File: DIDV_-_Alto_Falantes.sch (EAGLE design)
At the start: 32 parts, among them J101 JACKP2, J102 JACKP2, U101 LM386M, U102 LM386M

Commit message: Revisão 7:
-  Alterações necessárias para adequação às necessidades dos exemplos de controle que temos.
-  Revisão da forma de filtragem de sinais digitais
-  Algumas nomenclaturas ainda estão erradas, deverão ser corrigidas com o andamento da implementação.
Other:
- note added: "07"
- note removed: "01"
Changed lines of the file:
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@@
 <text x="203.2" y="29.464" size="1.778" layer="150" font="vector">Dispositivo de Interface para</text>
 <text x="210.82" y="26.162" size="1.778" layer="150" font="vector">Deficientes Visuais</text>
-<text x="250.698" y="10.16" size="2.54" layer="150" font="vector">01</text>
+<text x="250.698" y="10.16" size="2.54" layer="150" font="vector">07</text>
 <text x="7.62" y="7.62" size="2.54" layer="97" font="vector">Alimentacao 5V0</text>
 <wire x1="5.08" y1="45.72" x2="5.08" y2="5.08" width="0.1524" layer="150" style="longdash"/>

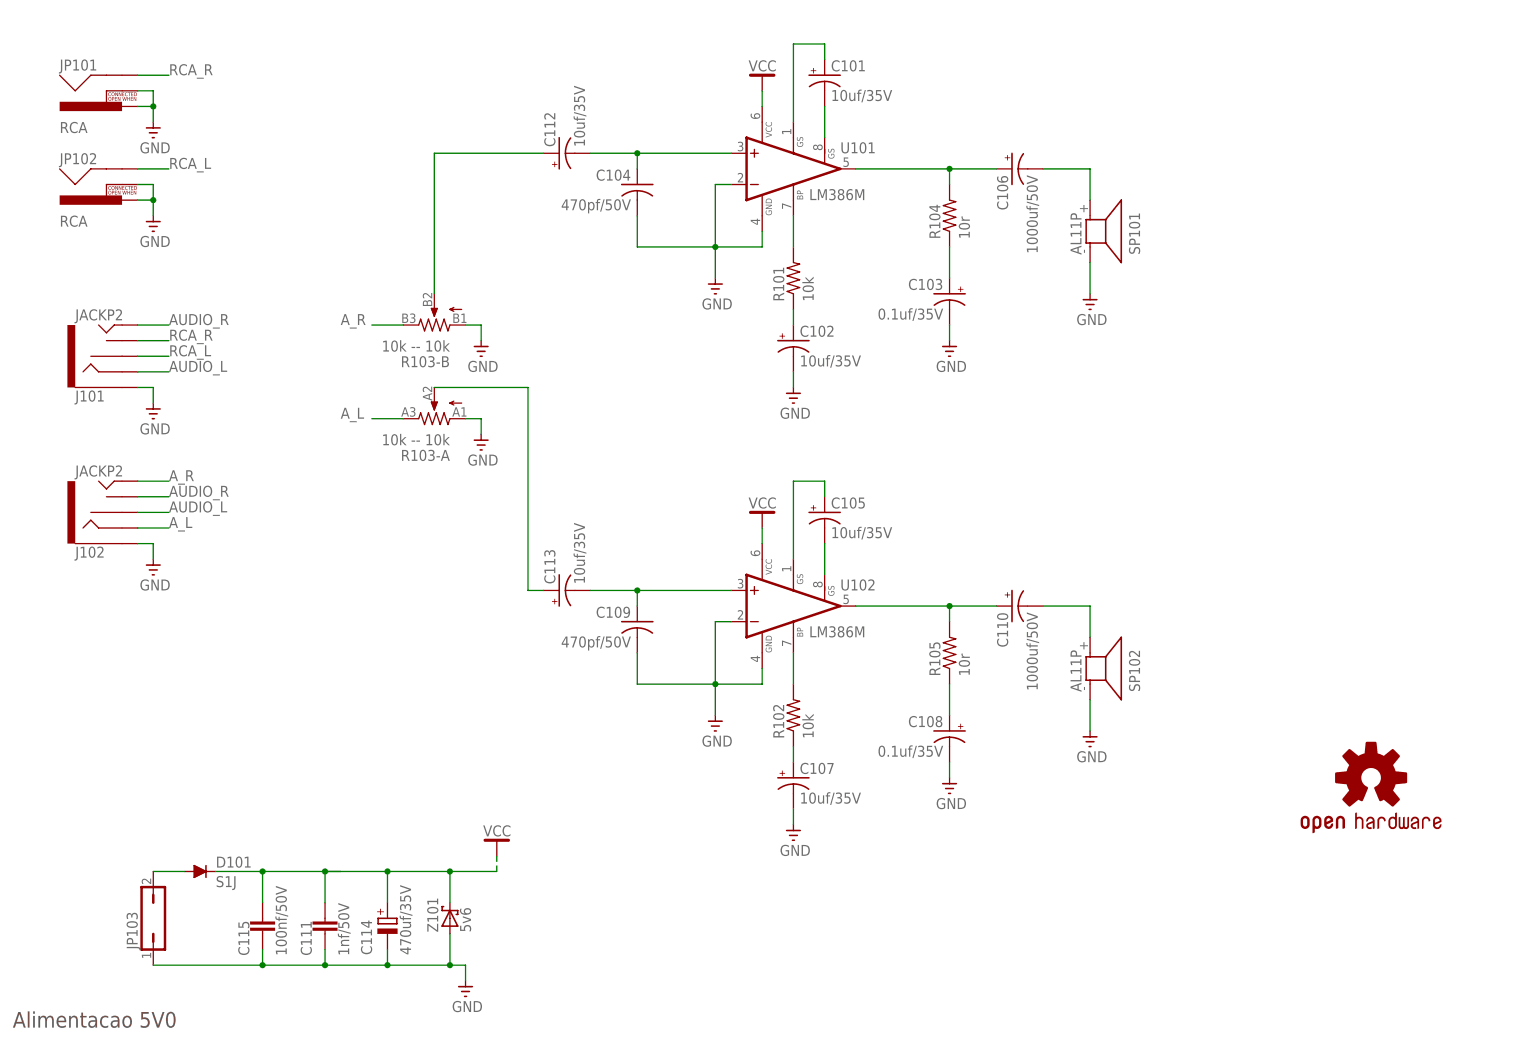
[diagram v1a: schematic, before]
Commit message: Revisão 8:
-  Add Circuito Buck
-  Alterações funcionais
-   Inserção dos primeiros boards
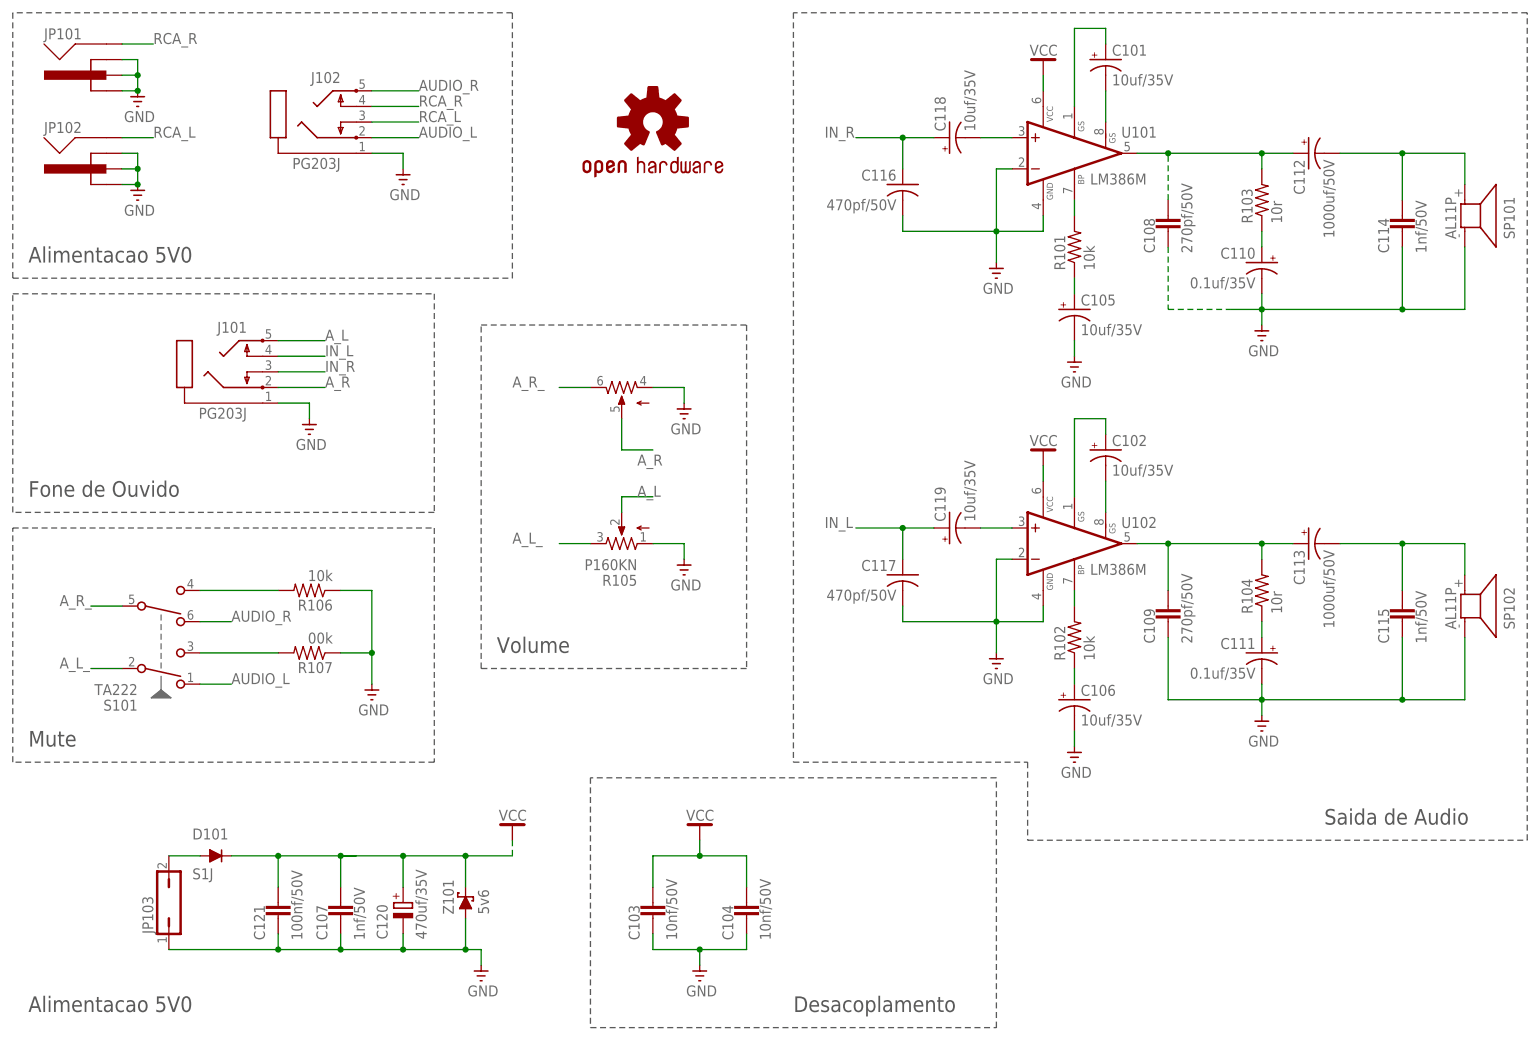
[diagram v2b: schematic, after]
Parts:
- added C116, C117: 470pf/50V, rcl:C-USC0603
- added C118, C119: 10uf/35V, resistor:CPOL-USE2-5
- added C120: 470uf/35V, rcl:CPOL-EUE3.5-10
- added C121: 100nf/50V, rcl:C-EUC0805
- added R106: 10k, rcl:R-US_R1206
- added R107: 00k, rcl:R-US_R1206
- added S101: TA222, switch-e-switch:TA222
- C103: value 0.1uf/35V -> 10nf/50V; device resistor:CPOL-USE2-5 -> rcl:C-EUC0805
- C104: value 470pf/50V -> 10nf/50V; device rcl:C-US025-025X050 -> rcl:C-EUC0805
- C106: value 1000uf/50V -> 10uf/35V; device resistor:CPOL-USE3.5-10 -> resistor:CPOL-USE2-5
- C107: value 10uf/35V -> 1nf/50V; device resistor:CPOL-USE2-5 -> rcl:C-EUC0805
- C108: value 0.1uf/35V -> 270pf/50V; device resistor:CPOL-USE2-5 -> rcl:C-EUC0805
- C109: value 470pf/50V -> 270pf/50V; device rcl:C-US025-025X050 -> rcl:C-EUC0805
- C110: value 1000uf/50V -> 0.1uf/35V; device resistor:CPOL-USE3.5-10 -> resistor:CPOL-USE2-5
- C111: value 1nf/50V -> 0.1uf/35V; device rcl:C-EUC0805 -> resistor:CPOL-USE2-5
- C112, C113: value 10uf/35V -> 1000uf/50V; device resistor:CPOL-USE2-5 -> resistor:CPOL-USE3.5-10
- C114: value 470uf/35V -> 1nf/50V; device rcl:CPOL-EUE3.5-10 -> rcl:C-EUC0805
- C115: value 100nf/50V -> 1nf/50V
- J101, J102: value JACKP2 -> PG203J; device SparkFun-Connectors:AUDIO-JACK2KIT -> con-hirschmann:PG203J; PROD_ID CONN-08774 -> (none)
- JP101, JP102: value RCA -> (none); device SparkFun-Connectors:RCA -> RCA_Hikichi:RCA
- LOGO101: value OSHW-LOGOM -> OSHW-LOGOL; device SparkFun-Aesthetics:OSHW-LOGOM -> OpenHW_BOT:OSHW-LOGOL
- R103: value 10k -- 10k -> 10r; device pot:P082N -> rcl:R-US_R1206
- R105: value 10r -> P160KN; device rcl:R-US_R1206 -> pot_hikichi:P160KN
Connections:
- removed net N$19: C113.+, R103-A.2
- removed net N$20: C112.+, R103-B.2
- new net A_L_: R105.3, S101.A-COM
- new net A_R_: R105.5, S101.B-COM
- new net IN_L: C117.1, C119.+, J101.4
- new net IN_R: C116.1, C118.+, J101.3
- new net N$10: R106.2, S101.B-NO
- new net N$18: R107.2, S101.A-NO
- net AUDIO_L: now also J102.2, S101.A-NC; no longer J101.RING, J102.RSH
- net AUDIO_R: now also J102.5, S101.B-NC; no longer J101.TIP, J102.TSH
- net A_L: now also J101.5, R105.2; no longer J102.RING, R103-A.3
- net A_R: now also J101.2, R105.6; no longer J102.TIP, R103-B.3
- net GND: now also C103.2, C105.-, C106.-, C107.2, C108.2, C110.-, C111.-, C114.2, C116.2, C117.2, C120.-, C121.2, J101.1, J102.1, JP101.GND, JP101.GND1, JP101.GND2, JP102.GND, JP102.GND1, JP102.GND2, R105.1, R105.4, R106.1, R107.1; no longer C102.-, C103.-, C107.-, C108.-, C111.2, C114.-, J101.SLEEVE, J102.SLEEVE, JP101.PIN, JP101.SWITCH, JP102.PIN, JP102.SWITCH, R103-A.1, R103-B.1
- net N$1: now also C105.+; no longer C102.+
- net N$11: now also C106.+; no longer C107.+
- net N$13: now also C111.+, R104.1; no longer C108.+, R105.1
- net N$14: now also C109.1, C113.+, R104.2; no longer C110.+, R105.2
- net N$15: now also C102.-; no longer C105.-
- net N$16: now also C102.+; no longer C105.+
- net N$17: now also C119.-; no longer C109.1, C113.-
- net N$3: now also C110.+, R103.1; no longer C103.+, R104.1
- net N$4: now also C108.1, C112.+, R103.2; no longer C106.+, R104.2
- net N$7: now also C118.-; no longer C104.1, C112.-
- net N$8: now also C113.-, C115.1; no longer C110.-
- net N$9: now also C112.-, C114.1; no longer C106.-
- net RCA_L: now also J102.3, JP102.SIGNAL; no longer J101.RSH, JP102.SHELL
- net RCA_R: now also J102.4, JP101.SIGNAL; no longer J101.TSH, JP101.SHELL
- net VCC: now also C103.1, C104.1, C107.1, C120.+, C121.1; no longer C111.1, C114.+, C115.1
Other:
- note added: "08"
- note added: "Desacoplamento"
- note added: "Fone de Ouvido"
- note added: "Mute"
- note added: "Saida de Audio"
- note added: "Volume"
- note removed: "07"
- moved on the sheet: C101, C102, C104, C105, C106, C109, C110, C112, C113, C115, D101, JP103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

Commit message: Revisão 9
- Corrigidos algumas falhas de ligação
- Implementação com VPRG dos TLCs via Hardware
- Inserção do cálculo do Riref

Obs. Se somente a criação de boards, não será incrementado. No caso, se criado um board novo board vou subir para 9.1 e assim por diante.
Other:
- note added: "09"
- note removed: "08"
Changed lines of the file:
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@@
 <text x="203.2" y="29.464" size="1.778" layer="150" font="vector">Dispositivo de Interface para</text>
 <text x="210.82" y="26.162" size="1.778" layer="150" font="vector">Deficientes Visuais</text>
-<text x="250.698" y="10.16" size="2.54" layer="150" font="vector">08</text>
+<text x="250.698" y="10.16" size="2.54" layer="150" font="vector">09</text>
 <text x="10.16" y="10.16" size="2.54" layer="97" font="vector">Alimentacao 5V0</text>
 <wire x1="7.62" y1="48.26" x2="7.62" y2="7.62" width="0.1524" layer="150" style="longdash"/>

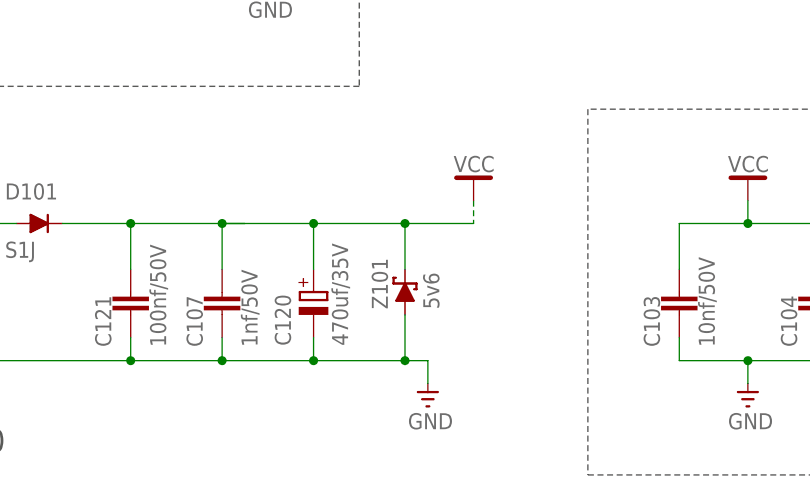
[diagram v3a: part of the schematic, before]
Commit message: Revisão 10
Revisão representa o estado final do projeto, alterações agora somente referentes a valores de componentes e adaptações se e somente se não existir a possibilidade de manobras via software.

Placas nas dimensões e condições as quais foram submetidas a cotação para confecção em local especializado.
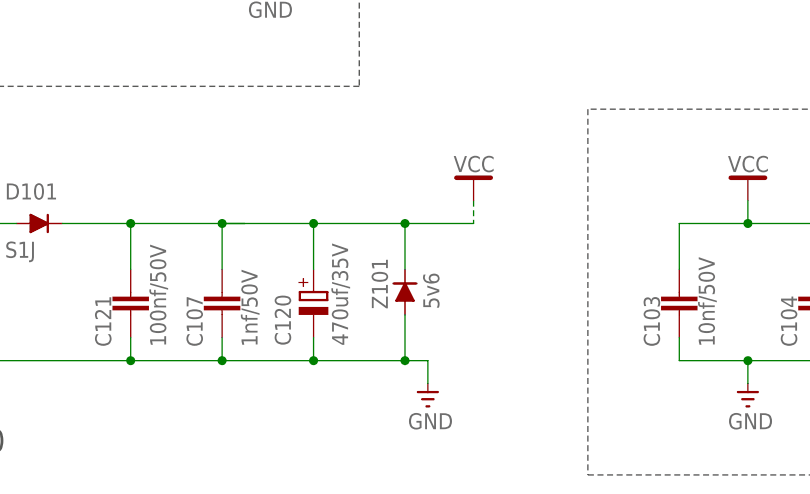
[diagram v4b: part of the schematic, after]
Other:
- note added: "10"
- note removed: "09"
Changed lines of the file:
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@@
 <text x="203.2" y="29.464" size="1.778" layer="150" font="vector">Dispositivo de Interface para</text>
 <text x="210.82" y="26.162" size="1.778" layer="150" font="vector">Deficientes Visuais</text>
-<text x="250.698" y="10.16" size="2.54" layer="150" font="vector">09</text>
+<text x="250.698" y="10.16" size="2.54" layer="150" font="vector">10</text>
 <text x="10.16" y="10.16" size="2.54" layer="97" font="vector">Alimentacao 5V0</text>
 <wire x1="7.62" y1="48.26" x2="7.62" y2="7.62" width="0.1524" layer="150" style="longdash"/>
